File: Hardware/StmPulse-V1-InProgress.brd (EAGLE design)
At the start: 60.3 x 128.5 mm, 58 parts, among them IC1 78M05, IC2 MCP6004D, U1 MCP6004D, U2-MCP4922 MCP4922MCP4922-SO14

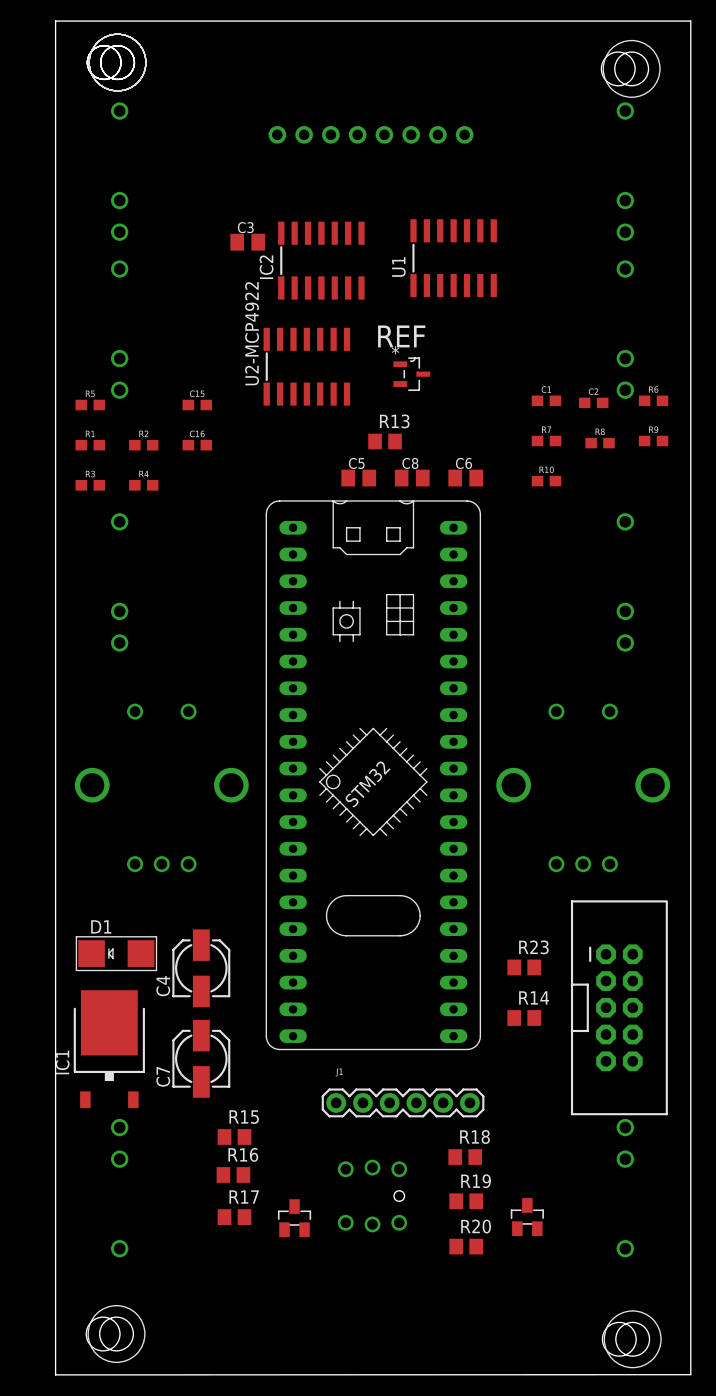
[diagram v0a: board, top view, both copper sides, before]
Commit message: moved mounting holes
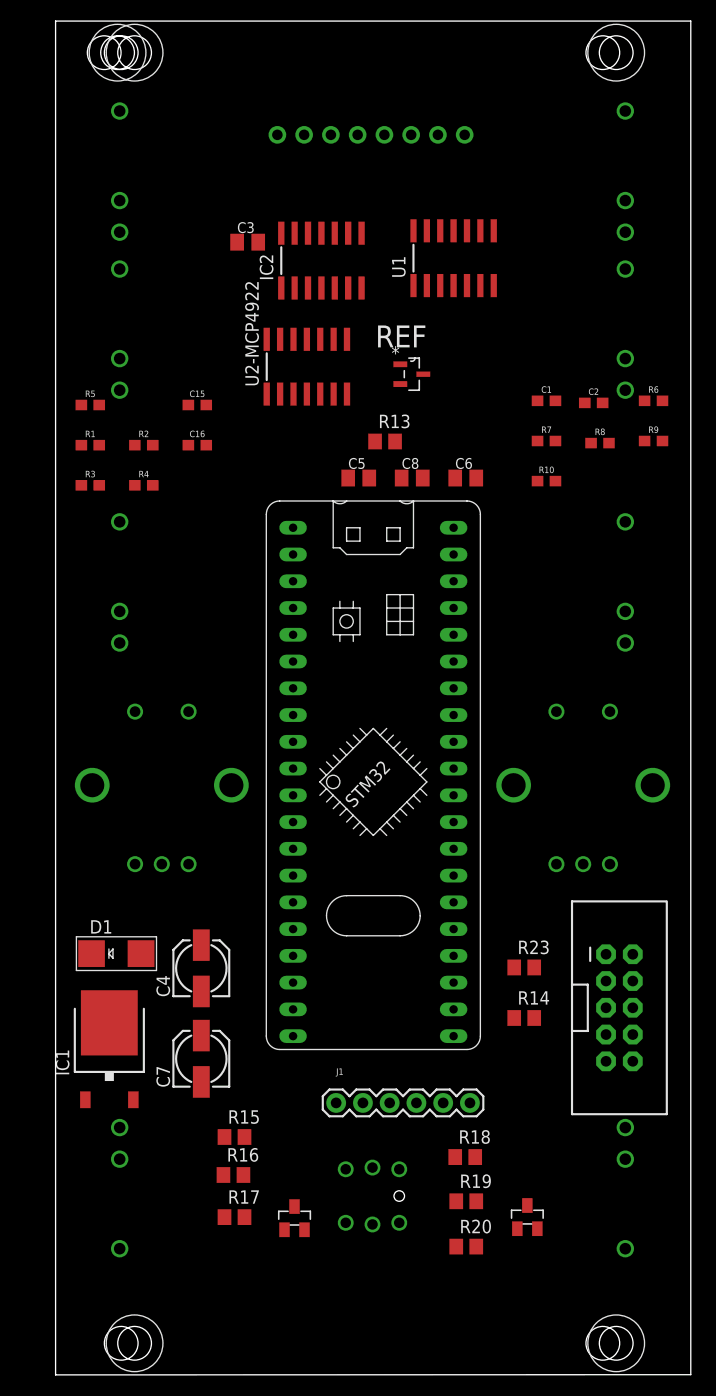
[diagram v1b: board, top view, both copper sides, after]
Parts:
- removed U$6: (no value), GMSN-R2Project:MOUNTING_HOLE
- moved U$4 2.13 mm to (131.1, 94.5)
- moved U$2 1.93 mm to (85.4, -28.0)
- moved U$7 1.87 mm to (85.4, 94.5)
- moved U$3 1.61 mm to (131.1, -28.0)
- moved U$5 0.94 mm to (83.8, 94.5)
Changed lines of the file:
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@@
 <attribute name="VALUE" x="94.477" y="19.92" size="0.6096" layer="28" font="vector" ratio="20" rot="MR270" align="top-center"/>
 </element>
-<element name="U$2" library="GMSN-R2Project" package="MOUNTING_HOLE" value="" x="83.7" y="-27.1" smashed="yes" rot="R90"/>
-<element name="U$3" library="GMSN-R2Project" package="MOUNTING_HOLE" value="" x="132.7" y="-27.6" smashed="yes" rot="R90"/>
-<element name="U$4" library="GMSN-R2Project" package="MOUNTING_HOLE" value="" x="132.6" y="93" smashed="yes" rot="R90"/>
-<element name="U$5" library="GMSN-R2Project" package="MOUNTING_HOLE" value="" x="83.8" y="93.6" smashed="yes" rot="R90"/>
-<element name="U$6" library="GMSN-R2Project" package="MOUNTING_HOLE" value="" x="83.8" y="93.6" smashed="yes" rot="R90"/>
-<element name="U$7" library="GMSN-R2Project" package="MOUNTING_HOLE" value="" x="83.8" y="93.6" smashed="yes" rot="R90"/>
+<element name="U$2" library="GMSN-R2Project" package="MOUNTING_HOLE" value="" x="85.415" y="-27.98" smashed="yes" rot="R90"/>
+<element name="U$3" library="GMSN-R2Project" package="MOUNTING_HOLE" value="" x="131.135" y="-27.98" smashed="yes" rot="R90"/>
+<element name="U$4" library="GMSN-R2Project" package="MOUNTING_HOLE" value="" x="131.135" y="94.54" smashed="yes" rot="R90"/>
+<element name="U$5" library="GMSN-R2Project" package="MOUNTING_HOLE" value="" x="83.8" y="94.54" smashed="yes" rot="R90"/>
+<element name="U$7" library="GMSN-R2Project" package="MOUNTING_HOLE" value="" x="85.415" y="94.54" smashed="yes" rot="R90"/>
 </elements>
 <signals>

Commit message: Changed C and R to 805
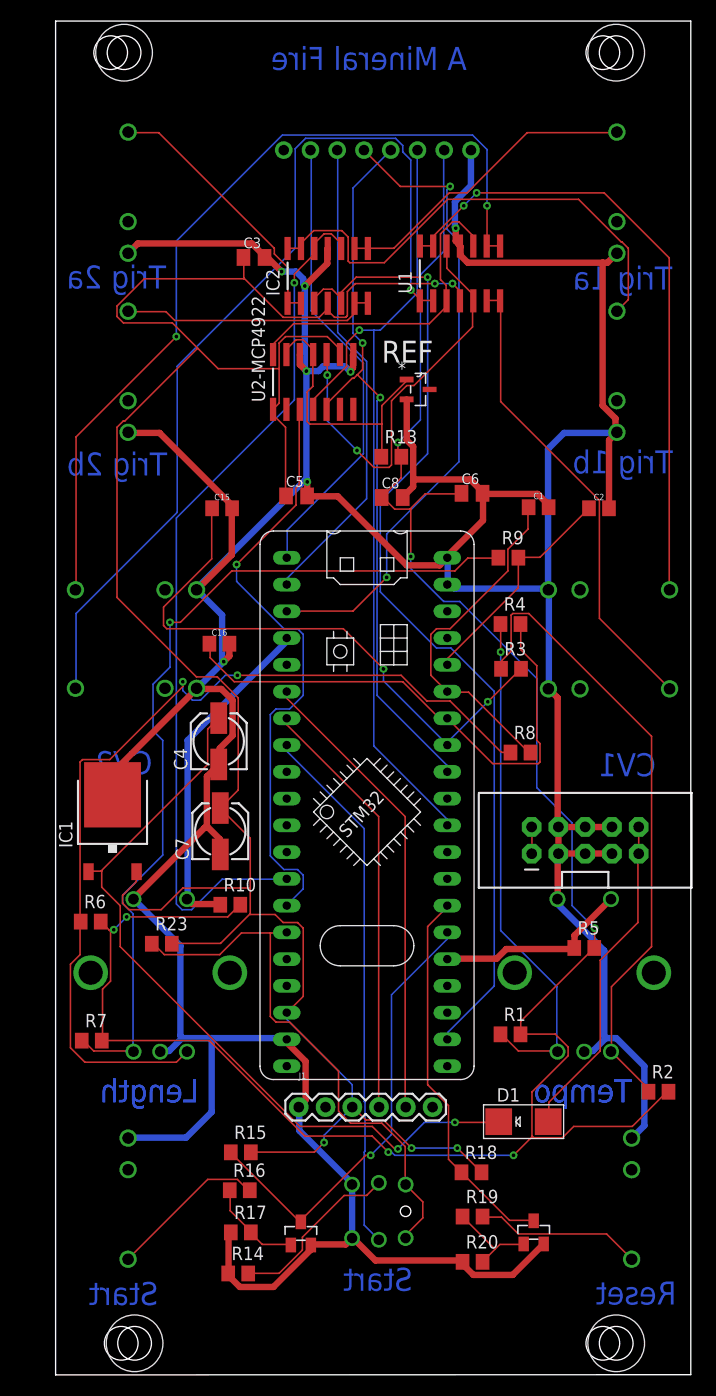
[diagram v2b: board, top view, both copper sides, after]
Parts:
- removed U$7: (no value), GMSN-R2Project:MOUNTING_HOLE
- added CV3, CV4: S_JACK, INSTRUO:S_JACK
- C1, C15, C16, C2: device SparkFun-Capacitors:0603 -> rcl:C0805
- CLOCK1: value 2N3904 -> TRANSISTOR_MMBT3904
- R1, R10, R2, R3, R4, R5, R6, R7, R8, R9: value 10k -> 10K; device SparkFun-Resistors:0603 -> rcl:R0805
- moved R2 78.5 mm to (135.2, -4.10)
- moved R6 72.8 mm to (81.2, 12.1)
- moved R7 71.4 mm to (81.3, 0.75)
- moved R5 69.7 mm to (128.1, 9.55)
- moved R1 68.7 mm to (121.1, 1.35)
- moved R10 50.2 mm to (94.5, 13.7)
- moved R3 43.6 mm to (121.2, 36.0)
- moved D1 41.8 mm to (122.3, -6.94)
- moved R4 37.2 mm to (121.1, 40.3)
- moved R14 36.4 mm to (95.2, -21.4)
- moved R23 34.5 mm to (88.0, 9.95)
- moved R8 30.3 mm to (122.0, 28.1)
- moved C7 21.7 mm to (93.5, 20.6)
- moved IC1 21.7 mm to (83.3, 21.6)
- moved C4 21.6 mm to (93.4, 29.2)
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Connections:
- new net N$4: CV3.TIP, U1.1, U1.2
- new net N$5: CV4.TIP, U1.6, U1.7
- net GND: now also CV3.GND, CV4.GND
- net N$1: now also R6.1; no longer R7.1
- net N$2: now also R7.1; no longer R6.1
- net VOUTA: now also U1.3
- net VOUTB: now also U1.5
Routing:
- net GND: track 0.00 -> 451.8 mm, vias 0 -> 7
- net +5V: track 0.00 -> 226.3 mm, vias 0 -> 5
- net 5V: track 0.00 -> 206.7 mm, vias 0 -> 7
- net TRIG2: track 0.00 -> 95.5 mm, vias 0 -> 1
- net N$1: track 0.00 -> 89.1 mm, vias 0 -> 2
- net N$4: track 0.00 -> 87.5 mm, vias 0 -> 1
- net TRIG1: track 0.00 -> 83.8 mm, vias 0 -> 1
- net N$2: track 0.00 -> 82.9 mm, vias 0 -> 1
- net N$11: track 0.00 -> 81.8 mm, vias 0 -> 2
- net SCK: track 0.00 -> 79.8 mm, vias 0 -> 1
- net +12V: track 0.00 -> 73.3 mm, vias 0 -> 2
- net MOSI: track 0.00 -> 69.5 mm, vias 0 -> 2
- net RST_DISP: track 0.00 -> 61.0 mm, vias 0 -> 2
- net N$6: track 0.00 -> 60.5 mm
- net N$36: track 0.00 -> 60.4 mm, vias 0 -> 2
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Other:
- board text added: "A Mineral Fire"
- board text added: "CC BY 3.0"
- board text added: "CV1"
- board text added: "CV2"
- board text added: "Length"
- board text added: "Reset"
- board text added: "Sequencer Design Andy C"
- board text added: "Start"
- board text added: "Tempo"
- board text added: "Trig 1a"
- board text added: "Trig 1b"
- board text added: "Trig 2a"
- board text added: "Trig 2b"
- board text added: "V1.0"

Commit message: Updated encoder switches
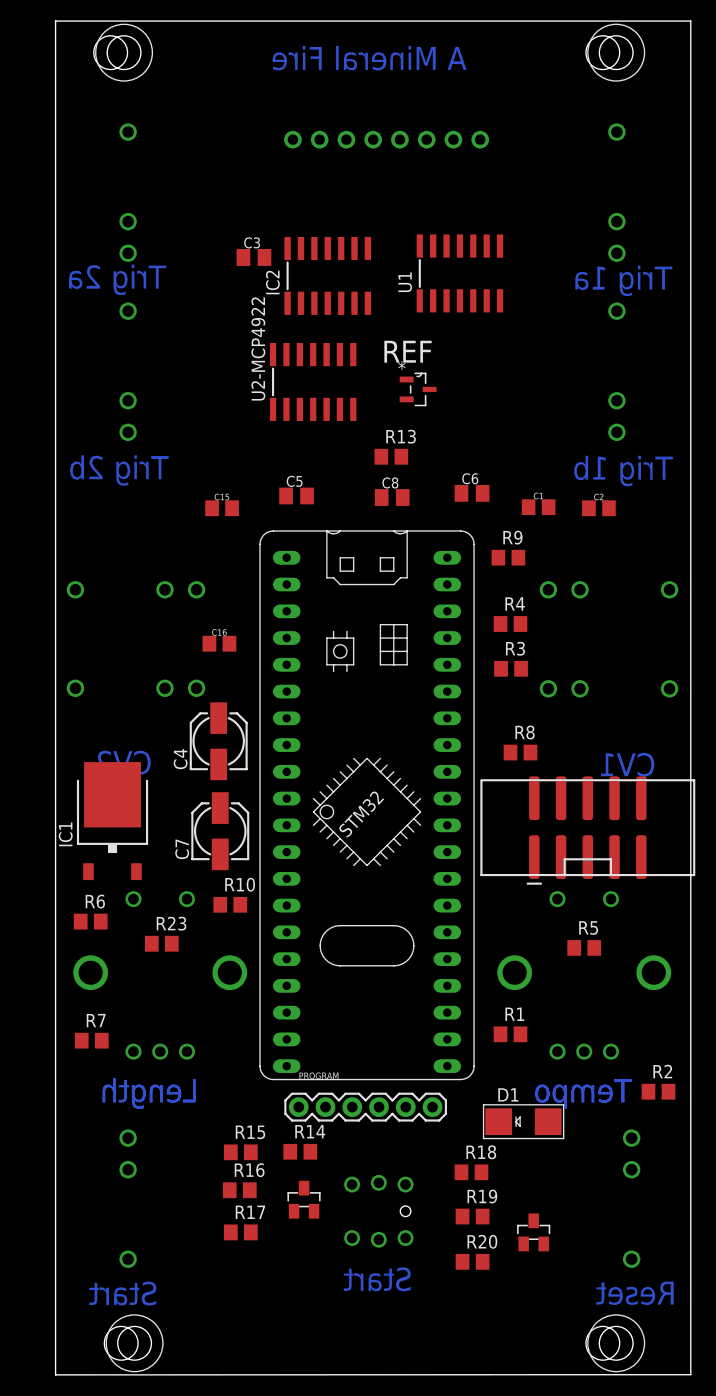
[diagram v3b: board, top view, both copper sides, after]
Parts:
- removed JP1: (no value), Adafruit_1.3_128x64_OLED:MICROBUILDER_1X08_ROUND
- added DISPLAY: (no value), Adafruit_1.3_128x64_OLED:MICROBUILDER_1X08_ROUND
- POWER: value HEADER2X5SHD -> (none); device GMSN:2X5-SHROUDED -> SparkFun-Connectors:2X5-SHROUDED_SMD
- PROGRAM: value (none) -> Program
- moved R14 13.0 mm to (101.2, -9.80)
- moved CLOCK 3.21 mm to (101.5, -14.3)
- moved POWER 1.23 mm to (128.4, 21.0)
- renumbered J1 to PROGRAM
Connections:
- net +5V: now also C6.1, C8.1, DISPLAY.2, R13.2
- net 5V: no longer C6.1, C8.1, JP1.2, R13.2
- net CS_DISP: now also DISPLAY.7; no longer JP1.7
- net DC_DISP: now also DISPLAY.6; no longer JP1.6
- net GND: now also DISPLAY.1; no longer JP1.1
- net MOSI: now also DISPLAY.4; no longer JP1.4
- net RST_DISP: now also DISPLAY.5; no longer JP1.5
- net SCK: now also DISPLAY.3; no longer JP1.3
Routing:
- net GND: track 451.8 -> 0.00 mm, vias 7 -> 0
- net +5V: track 226.3 -> 0.00 mm, vias 5 -> 0
- net 5V: track 206.7 -> 0.00 mm, vias 7 -> 0
- net TRIG2: track 95.5 -> 0.00 mm, vias 1 -> 0
- net N$1: track 89.1 -> 0.00 mm, vias 2 -> 0
- net N$4: track 87.5 -> 0.00 mm, vias 1 -> 0
- net TRIG1: track 83.8 -> 0.00 mm, vias 1 -> 0
- net N$2: track 82.9 -> 0.00 mm, vias 1 -> 0
- net N$11: track 81.8 -> 0.00 mm, vias 2 -> 0
- net SCK: track 79.8 -> 0.00 mm, vias 1 -> 0
- net +12V: track 73.3 -> 0.00 mm, vias 2 -> 0
- net MOSI: track 69.5 -> 0.00 mm, vias 2 -> 0
- net RST_DISP: track 61.0 -> 0.00 mm, vias 2 -> 0
- net N$6: track 60.5 -> 0.00 mm
- net N$36: track 60.4 -> 0.00 mm, vias 2 -> 0
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
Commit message: updated hardware
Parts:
- R14: value 330R -> 220R
- moved R15 2.44 mm to (93.2, -8.90)
- moved R16 2.33 mm to (93.2, -14.3)
- moved R17 1.97 mm to (97.2, -18.4)
- moved BUT3 0.53 mm to (108.1, -15.4)
- moved R5 0.32 mm to (128.4, 9.65)
- renumbered CLOCK to T1_CLOCK, CLOCK1 to T2_RESET
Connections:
- net BUTLED3: now also U$1.P$9; no longer U$1.P$8
